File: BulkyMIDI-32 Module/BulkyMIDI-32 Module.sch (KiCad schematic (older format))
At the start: 23 parts, among them IC1 0.96_OLED, J1 DC IN, J2 C64_IEC, J3 C64_IEC, J4 Faceplate, M1 Mounting, M2 Mounting, M3 Mounting, M4 Mounting, SW1 SELECT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

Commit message: Schematic drafted
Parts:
- removed BZ1: Buzzer, Buzzers_Beepers:Buzzer_12x9.5RM7.6, symbol Device:Buzzer
- removed D2: DRIVE, LEDs:LED_D5.0mm, symbol Device:LED_Small
- removed J2, J3: C64_IEC, C64_IEC:C64_IEC, symbol C64_IEC:C64_IEC
- removed R7: 330, Resistors_THT:R_Axial_DIN0207_L6.3mm_D2.5mm_P10.16mm_Horizontal, symbol Device:R
- removed SW5: ADD, Buttons_Switches_THT:SW_Tactile_SPST_Angled_PTS645Vx39-2LFS, symbol Switch:SW_Push
- added A2: GY-PCM5102, clumsyMIDI:GY-PCM5102, symbol gy-pcm5102:GY-PCM5102
- added C3: 100n, Capacitor_THT:C_Rect_L7.0mm_W2.0mm_P5.00mm, symbol Device:C
- added C4: 100nF, Capacitor_THT:C_Rect_L7.0mm_W2.0mm_P5.00mm, symbol Device:C
- added C5: 100uF, Capacitor_THT:CP_Radial_D6.3mm_P2.50mm, symbol Device:CP1
- added C6: 470u 10V, Capacitor_THT:CP_Radial_D8.0mm_P3.50mm, symbol Device:CP1
- added D1: 1N4148, Diode_THT:D_DO-35_SOD27_P7.62mm_Horizontal, symbol Device:D
- added ENC1: KY-040, Connector_PinHeader_2.54mm:PinHeader_1x05_P2.54mm_Vertical, symbol BulkyMIDI:KY-040
- added J2: MIDI Out Jack, clumsyMIDI:MultiDIN5, symbol Connector:DIN-5_180degree
- added J3: MIDI In Jack, clumsyMIDI:MultiDIN5, symbol Connector:DIN-5_180degree
- added J5: MIDI Thru Jack, Connector_PinHeader_2.54mm:PinHeader_1x05_P2.54mm_Vertical, symbol Connector:DIN-5_180degree
- added J6: Serial, Connector_PinHeader_2.54mm:PinHeader_1x04_P2.54mm_Horizontal, symbol BulkyMIDI:Serial_Adapter
- added R1, R2, R4, R5, R6: 220, Resistors_THT:R_Axial_DIN0207_L6.3mm_D2.5mm_P10.16mm_Horizontal, symbol Device:R
- added R3: 1k, Resistors_THT:R_Axial_DIN0207_L6.3mm_D2.5mm_P10.16mm_Horizontal, symbol Device:R
- added U1: 74HCT14, Package_DIP:DIP-14_W7.62mm, symbol 74xx:74HC14
- added U2: H11L1M, Package_DIP:DIP-6_W7.62mm, symbol Isolator:H11L1
- J4: footprint Pin_Headers:Pin_Header_Straight_1x04_Pitch2.54mm -> Connector_PinSocket_2.54mm:PinSocket_1x04_P2.54mm_Vertical
- SW1: value SELECT -> SYNTH
- SW2: value UP -> ROM
- SW3: value DOWN -> VOL_DOWN
- SW4: value EXIT -> VOL_UP
- renumbered R6 to R8
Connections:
- net labels added: I2S_BCLK, I2S_DATA, I2S_LRCLK, RX_TTL, SW_DOWN, SW_ENC, SW_ROM, SW_SYNTH, SW_UP, TX_TTL
- net labels removed: C64_ATN, C64_CLK, C64_DATA, C64_RST, RPI_ATN, RPI_CLK_IN, RPI_CLK_OUT, RPI_DATA_IN, RPI_DATA_OUT, RPI_LED, RPI_PWR, RPI_RST, SW1, SW2, SW3, SW4, SW5
- wire segments 112 -> 173
- no-connect marks 17 -> 35
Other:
- note added: "Optional MIDI In circuit"
- note added: "Optional MIDI Out circuit"
- note added: "Optional MIDI Thru circuit"
- note added: "Optional RS-232 or Serial USB adapter"
- moved on the sheet: A1, C1, IC1, J1, JP1, JP2, R8, SW1, SW2, SW3, SW4

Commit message: Changed faceplate connector and PCB size
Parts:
- IC1: value 0.96_OLED -> 1.3_OLED; footprint i2c_oled:0.96_I2C_OLED -> i2c_oled:1.3_I2C_OLED_No_mounting
- J4: footprint Connector_PinSocket_2.54mm:PinSocket_1x04_P2.54mm_Vertical -> Connector_PinSocket_2.54mm:PinSocket_1x10_P2.54mm_Vertical; symbol Connector_Generic:Conn_01x04 -> BulkyMIDI:Conn_Faceplate
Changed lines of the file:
@@
 P 8650 7750
 F 0 "IC1" H 8650 7575 60  0000 C CNN
-F 1 "0.96_OLED" H 8625 7700 43  0000 C CNN
-F 2 "i2c_oled:0.96_I2C_OLED" H 8650 8375 60  0001 C CNN
+F 1 "1.3_OLED" H 8625 7700 43  0000 C CNN
+F 2 "i2c_oled:1.3_I2C_OLED_No_mounting" H 8650 8375 60  0001 C CNN
 F 3 "" H 8650 8375 60  0001 C CNN
 	1    8650 7750
@@
 L power:GND #PWR015
 U 1 1 5E3CE2EF
-P 1375 9975
-F 0 "#PWR015" H 1375 9725 50  0001 C CNN
-F 1 "GND" H 1375 9825 50  0000 C CNN
-F 2 "" H 1375 9975 50  0001 C CNN
-F 3 "" H 1375 9975 50  0001 C CNN
-	1    1375 9975
+P 1400 9975
+F 0 "#PWR015" H 1400 9725 50  0001 C CNN
+F 1 "GND" H 1400 9825 50  0000 C CNN
+F 2 "" H 1400 9975 50  0001 C CNN
+F 3 "" H 1400 9975 50  0001 C CNN
+	1    1400 9975
 	-1   0    0    -1
 $EndComp
 Wire Wire Line
-	1375 9975 1375 9900
-Wire Wire Line
-	1375 9900 1450 9900
+	1400 9975 1400 9900
+Wire Wire Line
+	1400 9900 1475 9900
 $Comp
 L Device:LED_Small D3
 U 1 1 5E3CE73B
-P 1550 9900
-F 0 "D3" H 1500 10025 50  0000 L CNN
-F 1 "POWER" H 1425 9825 50  0000 L CNN
-F 2 "LEDs:LED_D5.0mm" V 1550 9900 50  0001 C CNN
-F 3 "" V 1550 9900 50  0001 C CNN
-	1    1550 9900
+P 1575 9900
+F 0 "D3" H 1525 10025 50  0000 L CNN
+F 1 "POWER" H 1450 9825 50  0000 L CNN
+F 2 "LEDs:LED_D5.0mm" V 1575 9900 50  0001 C CNN
+F 3 "" V 1575 9900 50  0001 C CNN
+	1    1575 9900
 	1    0    0    1
 $EndComp
@@
 	1    0    0    -1
 $EndComp
-Wire Wire Line
-	1650 9900 1750 9900
-Wire Wire Line
-	2050 9900 2525 9900
 $Comp
 L Switch:SW_Push SW1
 U 1 1 5EE65CEA
 P 6050 6175
-F 0 "SW1" H 6050 6460 50  0000 C CNN
-F 1 "SYNTH" H 6050 6369 50  0000 C CNN
+F 0 "SW1" H 5975 6350 50  0000 C CNN
+F 1 "SYNTH" H 6100 6350 50  0000 L CNN
 F 2 "Buttons_Switches_THT:SW_Tactile_SPST_Angled_PTS645Vx39-2LFS" H 6050 6375 50  0001 C CNN
 F 3 "~" H 6050 6375 50  0001 C CNN
@@
 U 1 1 5EE67BD2
 P 6050 6575
-F 0 "SW2" H 6050 6860 50  0000 C CNN
-F 1 "ROM" H 6050 6769 50  0000 C CNN
+F 0 "SW2" H 5975 6775 50  0000 C CNN
+F 1 "ROM" H 6100 6775 50  0000 L CNN
 F 2 "Buttons_Switches_THT:SW_Tactile_SPST_Angled_PTS645Vx39-2LFS" H 6050 6775 50  0001 C CNN
 F 3 "~" H 6050 6775 50  0001 C CNN
@@
 U 1 1 5EE6919F
 P 6050 6975
-F 0 "SW3" H 6050 7260 50  0000 C CNN
-F 1 "VOL_DOWN" H 6050 7169 50  0000 C CNN
+F 0 "SW3" H 5975 7150 50  0000 C CNN
+F 1 "VOL_DOWN" H 6100 7150 50  0000 L CNN
 F 2 "Buttons_Switches_THT:SW_Tactile_SPST_Angled_PTS645Vx39-2LFS" H 6050 7175 50  0001 C CNN
 F 3 "~" H 6050 7175 50  0001 C CNN
@@
 U 1 1 5EE6A509
 P 6050 7375
-F 0 "SW4" H 6050 7660 50  0000 C CNN
-F 1 "VOL_UP" H 6050 7569 50  0000 C CNN
+F 0 "SW4" H 5975 7550 50  0000 C CNN
+F 1 "VOL_UP" H 6100 7550 50  0000 L CNN
 F 2 "Buttons_Switches_THT:SW_Tactile_SPST_Angled_PTS645Vx39-2LFS" H 6050 7575 50  0001 C CNN
 F 3 "~" H 6050 7575 50  0001 C CNN
@@
 L power:+3.3V #PWR0102
 U 1 1 5EE9DCDF
-P 2525 9825
-F 0 "#PWR0102" H 2525 9675 50  0001 C CNN
-F 1 "+3.3V" H 2540 9998 50  0000 C CNN
-F 2 "" H 2525 9825 50  0001 C CNN
-F 3 "" H 2525 9825 50  0001 C CNN
-	1    2525 9825
-	1    0    0    -1
-$EndComp
-Wire Wire Line
-	2525 9825 2525 9900
+P 2125 9825
+F 0 "#PWR0102" H 2125 9675 50  0001 C CNN
+F 1 "+3.3V" H 2140 9998 50  0000 C CNN
+F 2 "" H 2125 9825 50  0001 C CNN
+F 3 "" H 2125 9825 50  0001 C CNN
+	1    2125 9825
+	1    0    0    -1
+$EndComp
 Wire Wire Line
 	6325 6175 6250 6175
@@
 Wire Wire Line
 	8875 6725 9150 6725
-$Comp
-L Connector_Generic:Conn_01x04 J4
-U 1 1 5F3B6F1D
-P 10100 7025
-F 0 "J4" H 10180 7017 50  0000 L CNN
-F 1 "Faceplate" H 10180 6926 50  0000 L CNN
-F 2 "Connector_PinSocket_2.54mm:PinSocket_1x04_P2.54mm_Vertical" H 10100 7025 50  0001 C CNN
-F 3 "~" H 10100 7025 50  0001 C CNN
-	1    10100 7025
-	1    0    0    -1
-$EndComp
 Wire Wire Line
 	8725 7125 8725 7300
@@
 Wire Wire Line
 	8875 7225 9900 7225
-Wire Wire Line
-	9900 6925 9750 6925
-Wire Wire Line
-	9750 6925 9750 7300
-Wire Wire Line
-	9900 7025 9825 7025
-Wire Wire Line
-	9825 7025 9825 6800
 $Comp
 L power:GND #PWR0110
 U 1 1 5F4491DA
-P 9750 7300
-F 0 "#PWR0110" H 9750 7050 50  0001 C CNN
-F 1 "GND" H 9755 7127 50  0000 C CNN
-F 2 "" H 9750 7300 50  0001 C CNN
-F 3 "" H 9750 7300 50  0001 C CNN
-	1    9750 7300
+P 9350 7400
+F 0 "#PWR0110" H 9350 7150 50  0001 C CNN
+F 1 "GND" H 9355 7227 50  0000 C CNN
+F 2 "" H 9350 7400 50  0001 C CNN
+F 3 "" H 9350 7400 50  0001 C CNN
+	1    9350 7400
 	-1   0    0    -1
 $EndComp
@@
 L power:+3.3V #PWR0114
 U 1 1 5F44F08B
-P 9825 6800
-F 0 "#PWR0114" H 9825 6650 50  0001 C CNN
-F 1 "+3.3V" H 9840 6973 50  0000 C CNN
-F 2 "" H 9825 6800 50  0001 C CNN
-F 3 "" H 9825 6800 50  0001 C CNN
-	1    9825 6800
+P 9825 6950
+F 0 "#PWR0114" H 9825 6800 50  0001 C CNN
+F 1 "+3.3V" H 9840 7123 50  0000 C CNN
+F 2 "" H 9825 6950 50  0001 C CNN
+F 3 "" H 9825 6950 50  0001 C CNN
+	1    9825 6950
 	-1   0    0    -1
 $EndComp
@@
 Text GLabel 6325 6575 2    50   Output ~ 0
 SW_ROM
+Text GLabel 6325 7375 2    50   Output ~ 0
+SW_UP
 Text GLabel 6325 6975 2    50   Output ~ 0
-SW_UP
-Text GLabel 6325 7375 2    50   Output ~ 0
 SW_DOWN
 Wire Wire Line
@@
 Wire Wire Line
 	4675 8000 4675 7675
+Wire Wire Line
+	9350 7325 9350 7400
+Wire Wire Line
+	9900 7025 9825 7025
+Wire Wire Line
+	9825 7025 9825 6950
+Text GLabel 9900 7625 0    50   Input ~ 0
+SW_SYNTH
+Text GLabel 9900 7825 0    50   Input ~ 0
+SW_UP
+Wire Wire Line
+	9350 7325 9900 7325
+$Comp
+L BulkyMIDI:Conn_Faceplate J4
+U 1 1 5F3B6F1D
+P 10100 7425
+F 0 "J4" H 10050 8075 50  0000 L CNN
+F 1 "Faceplate" H 10050 8000 50  0000 L CNN
+F 2 "Connector_PinSocket_2.54mm:PinSocket_1x10_P2.54mm_Vertical" H 10100 7425 50  0001 C CNN
+F 3 "~" H 10100 7425 50  0001 C CNN
+	1    10100 7425
+	1    0    0    -1
+$EndComp
+Text GLabel 9900 7725 0    50   Input ~ 0
+SW_ROM
+Text GLabel 9900 7925 0    50   Input ~ 0
+SW_DOWN
+Text GLabel 9900 7525 0    50   Input ~ 0
+SW_ENC
+Wire Wire Line
+	2125 9825 2125 9900
+Wire Wire Line
+	2125 9900 2050 9900
+Wire Wire Line
+	1675 9900 1750 9900
 $EndSCHEMATC

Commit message: Changed DIN to match
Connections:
- wire segments 173 -> 175
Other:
- moved on the sheet: A1, ENC1, IC1, J3, J4, JP1, JP2, SW1, SW2, SW3, SW4

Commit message: Routed tracks
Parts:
- removed D3: POWER, LEDs:LED_D5.0mm, symbol Device:LED_Small
- removed R8: 330, Resistors_THT:R_Axial_DIN0207_L6.3mm_D2.5mm_P10.16mm_Horizontal, symbol Device:R
- added JP3: SW4_SEL, Jumper:SolderJumper-3_P1.3mm_Open_RoundedPad1.0x1.5mm, symbol I2C_OLED:PowerSelect
- added SYM1: DC_5V, BulkyMIDI-32:PWR_Specification, symbol BulkyMIDI:DC_5V
- A1: value Raspberry PI -> Raspberry PI 3B
- A2: footprint clumsyMIDI:GY-PCM5102 -> BulkyMIDI-32:GY-PCM5102
- C1: footprint Capacitors_THT:C_Disc_D4.7mm_W2.5mm_P5.00mm -> Capacitor_THT:C_Rect_L7.0mm_W2.0mm_P5.00mm
- C3: value 100n -> 100nF
- C6: value 470u 10V -> 470uF
- ENC1, J5: footprint Connector_PinHeader_2.54mm:PinHeader_1x05_P2.54mm_Vertical -> Connector_PinHeader_2.54mm:PinHeader_1x05_P2.54mm_Horizontal
- IC1: value 1.3_OLED -> OLED
- J2: value MIDI Out Jack -> MIDI OUT; footprint clumsyMIDI:MultiDIN5 -> BulkyMIDI-32:DIN5_MIDI
- J3: value MIDI In Jack -> MIDI IN; footprint clumsyMIDI:MultiDIN5 -> BulkyMIDI-32:DIN5_MIDI
- JP1, JP2: footprint wire_pads:OLED_SEL -> Jumper:SolderJumper-3_P1.3mm_Open_RoundedPad1.0x1.5mm
- R1, R2, R3, R4, R5, R6: footprint Resistors_THT:R_Axial_DIN0207_L6.3mm_D2.5mm_P10.16mm_Horizontal -> Resistor_THT:R_Axial_DIN0207_L6.3mm_D2.5mm_P10.16mm_Horizontal
- SW1, SW2, SW3, SW4: footprint Buttons_Switches_THT:SW_Tactile_SPST_Angled_PTS645Vx39-2LFS -> Button_Switch_THT:SW_Tactile_SPST_Angled_PTS645Vx39-2LFS
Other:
- note added: "5-pin connector for connecting up a rotary encoder such as the KY-040, note that we'll still need\nthe SYNTH/ROM buttons from the "simple_buttons" control scheme as well. Currently the board\ndoes not have any proper methods for mounting it, unless you're mounting the whole thing in a\nseparate case."
- note added: "Control scheme ("simple_buttons")"
- note added: "Control scheme ("simple_encoder")"
- note added: "MIDI IN (optional)"
- note added: "MIDI Out (optional)"
- note added: "MIDI THRU (optional)"
- note added: "OLED display and faceplate connector"
- note added: "OLED displays have unfortunately been produced with varying pinouts, we therefore need to add solder\nbridges to specify what the pins are used for. Faceplate connector includes signals for both screen\nand control scheme pins, just in case a specific faceplate reimplements them in some way."
- note added: "Power section"
- note added: "RS-232 or TTL Serial USB adapter (optional)"
- note added: "Volume UP/DOWN is not needed when rotary encoder is\nused, some versions of faceplates may include SYNTH and\nVOL_UP and the duplicated switch should not be installed.\nJP3 is used to have the ROM switch replace VOL_UP."
- note removed: "Optional MIDI In circuit"
- note removed: "Optional MIDI Out circuit"
- note removed: "Optional MIDI Thru circuit"
- note removed: "Optional RS-232 or Serial USB adapter"
- moved on the sheet: A1, A2, C1, C3, C4, C5, C6, D1, ENC1, IC1, J1, J2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

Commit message: Changed port cutout to fit Raspberry Pi 4
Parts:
- A1: value Raspberry PI 3B -> Raspberry PI
- JP3: symbol I2C_OLED:PowerSelect -> Jumper:SolderJumper_3_Open
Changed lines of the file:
@@
 Title "BulkyMIDI-32 Module"
 Date ""
-Rev "A"
+Rev "B"
 Comp ""
 Comment1 ""
@@
 P 2875 3250
 F 0 "A1" H 2250 4600 50  0000 C CNN
-F 1 "Raspberry PI 3B" H 2250 4525 50  0000 C CNN
+F 1 "Raspberry PI" H 2250 4525 50  0000 C CNN
 F 2 "RPI:Raspberry_Pi_3B_Socketed_THT_FaceDown_MountingHoles" H 2875 3250 50  0001 C CNN
 F 3 "https://www.raspberrypi.org/documentation/hardware/raspberrypi/schematics/rpi_SCH_3bplus_1p0_reduced.pdf" H 2875 3250 50  0001 C CNN
@@
 Volume UP/DOWN is not needed when rotary encoder is\nused, some versions of faceplates may include SYNTH and\nVOL_UP and the duplicated switch should not be installed.\nJP3 is used to have the ROM switch replace VOL_UP.
 $Comp
-L I2C_OLED:PowerSelect JP3
+L Jumper:SolderJumper_3_Open JP3
 U 1 1 62208552
 P 10450 7925

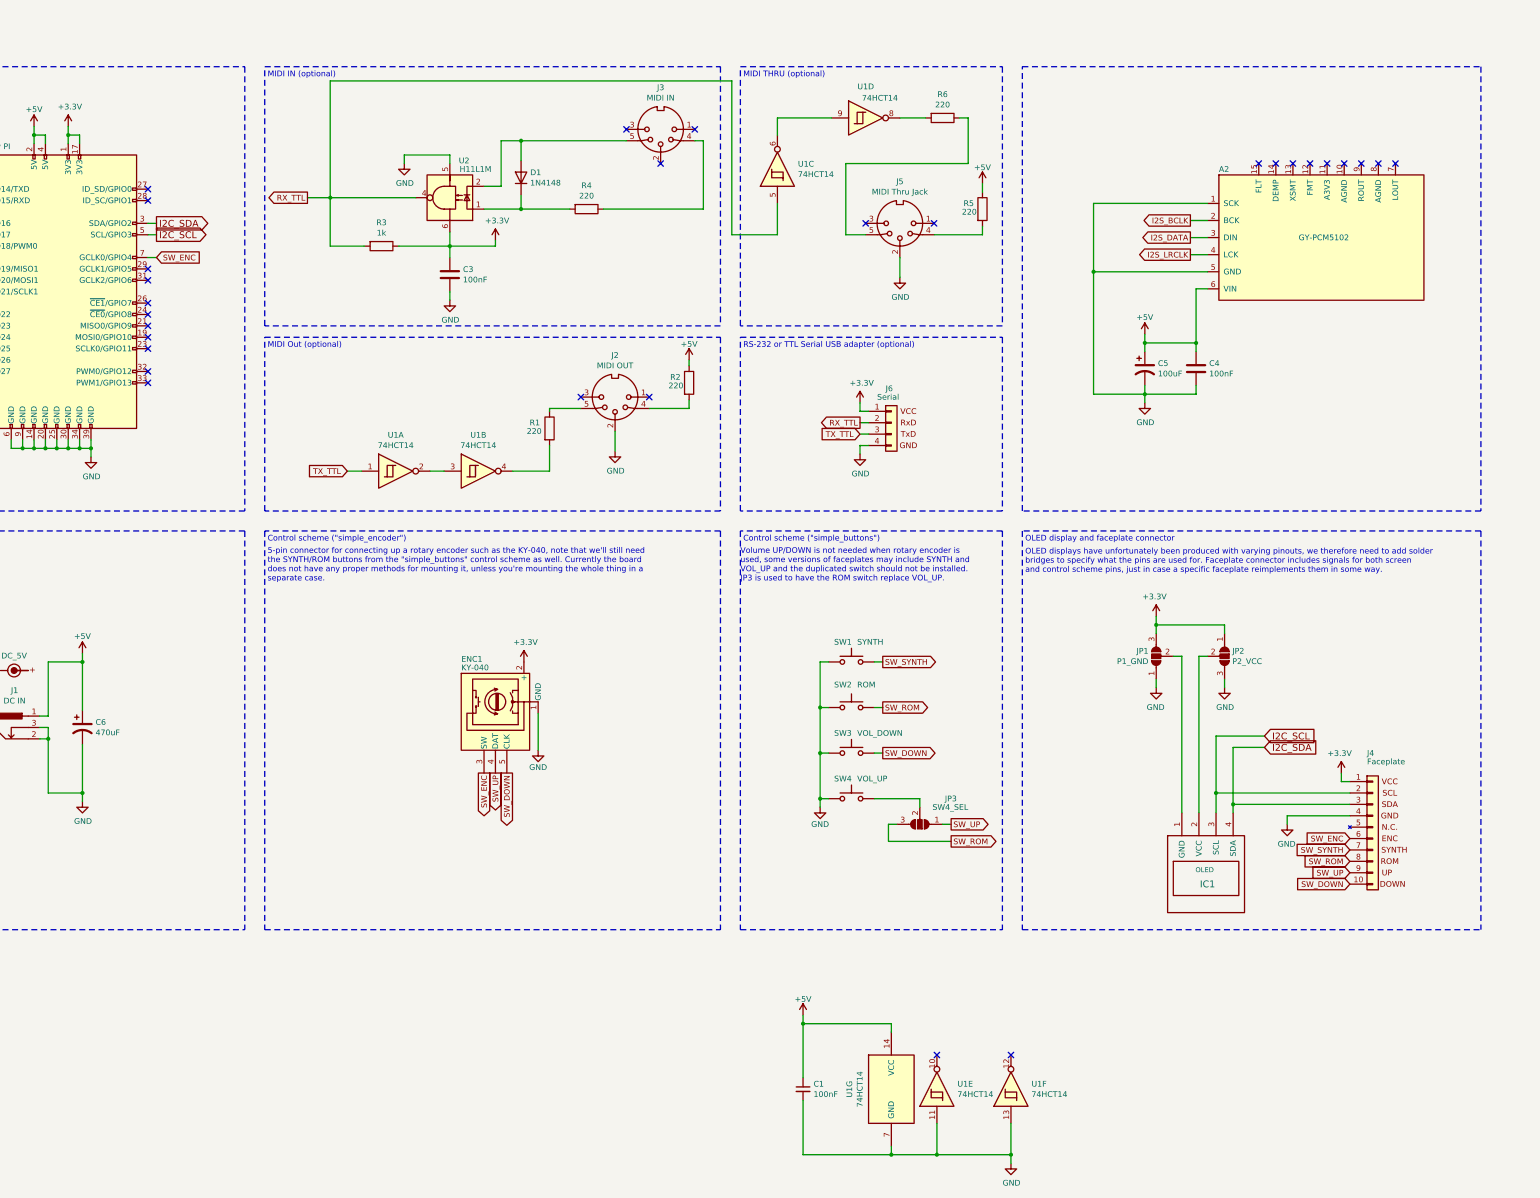
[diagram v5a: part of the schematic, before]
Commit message: Added extras connector
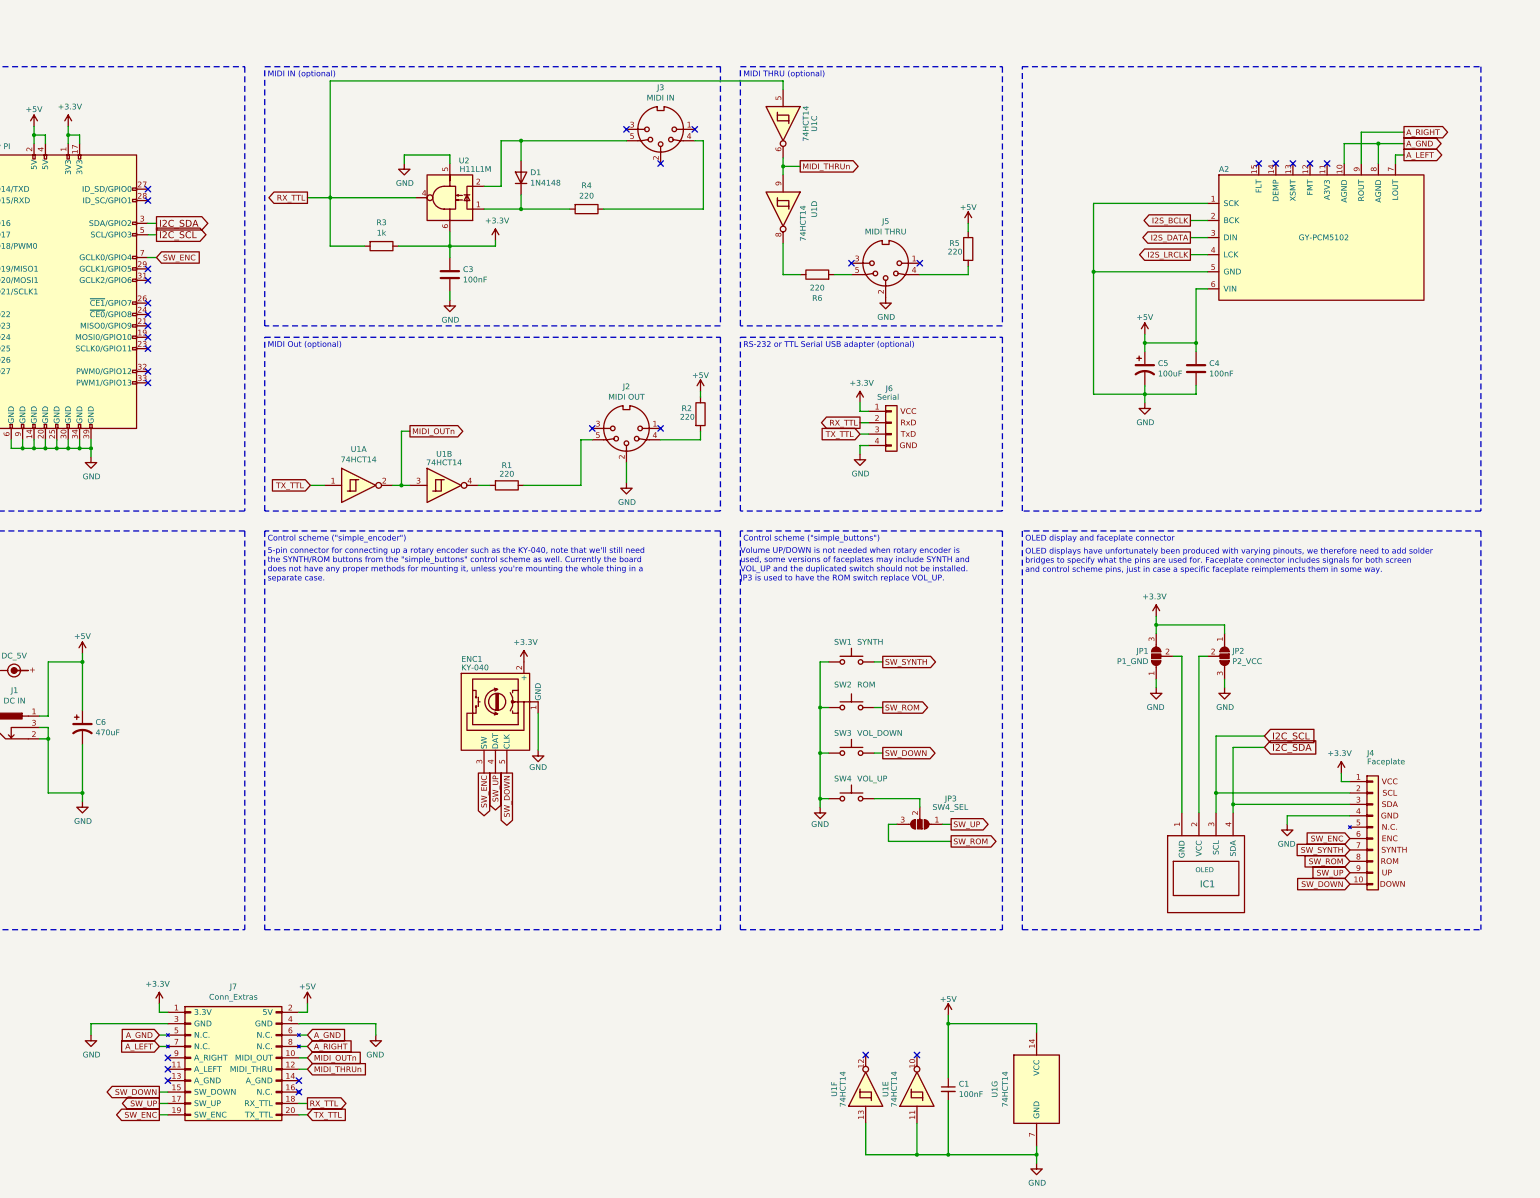
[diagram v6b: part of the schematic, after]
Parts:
- added J7: Conn_Extras, Connector_PinSocket_2.54mm:PinSocket_2x10_P2.54mm_Vertical, symbol BulkyMIDI:Conn_Extras
- J5: value MIDI Thru Jack -> MIDI THRU
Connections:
- net +3V3: now also J7.1 (3.3V)
- net +5V: now also J7.2 (5V)
- net GND: now also J7.3 (GND), J7.4 (GND)
- net RX_TTL: now also J7.18 (RX_TTL)
- net SW_DOWN: now also J7.15 (SW_DOWN)
- net SW_ENC: now also J7.19 (SW_ENC)
- net SW_UP: now also J7.17 (SW_UP)
- net TX_TTL: now also J7.20 (TX_TTL)
- net A_GND: now reaches A2.10 (AGND)
- net A_GND: now also A2.8 (AGND), J7.5 (N.C.), J7.6 (N.C.)
- net A_LEFT: now reaches A2.7 (LOUT)
- net A_LEFT: now also J7.7 (N.C.)
- net A_RIGHT: now reaches A2.9 (ROUT)
- net A_RIGHT: now also J7.8 (N.C.)
- net MIDI_OUTn: now reaches U1.2, U1.3
- net MIDI_OUTn: now also J7.10 (MIDI_OUT)
- net MIDI_THRUn: now reaches U1.6, U1.9
- net MIDI_THRUn: now also J7.12 (MIDI_THRU)
- net at U1.8: now also R6.1; no longer R6.2
- net at J5.5: now also R6.2; no longer R6.1
- no-connect marks 35 -> 36
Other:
- moved on the sheet: C1, J2, J5, R1, R2, R5, R6, U1A, U1B, U1C, U1D, U1E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
